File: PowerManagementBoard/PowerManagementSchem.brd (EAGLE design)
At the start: 160 x 100 mm, 29 parts, among them J1 D15S24A4GV00LF, U1 VX7805-500, U2 PYB20-Q24-S5, U3 PYB30-Q48-S5, U4 PYB30-Q48-S12, U5 3V3REG

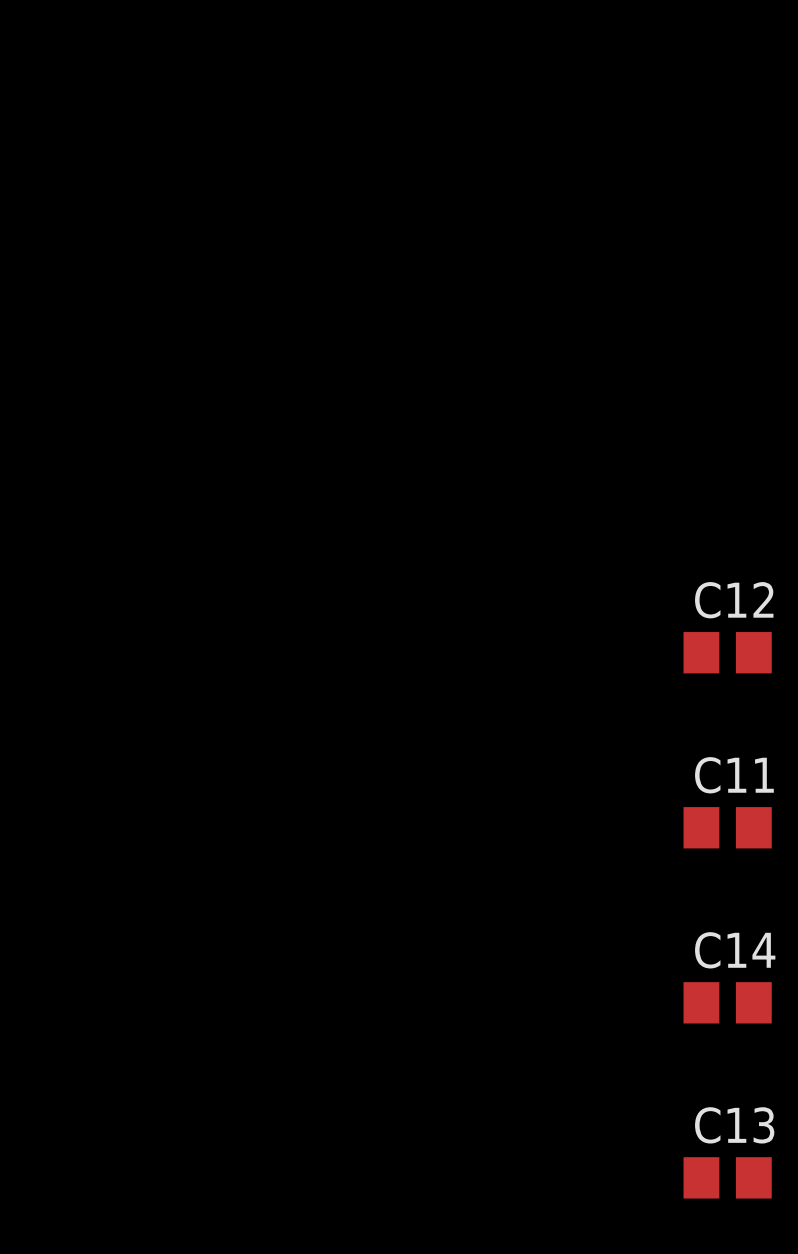
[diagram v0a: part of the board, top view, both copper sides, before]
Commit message: Added MOSFET to lib. Added Teensy to schem
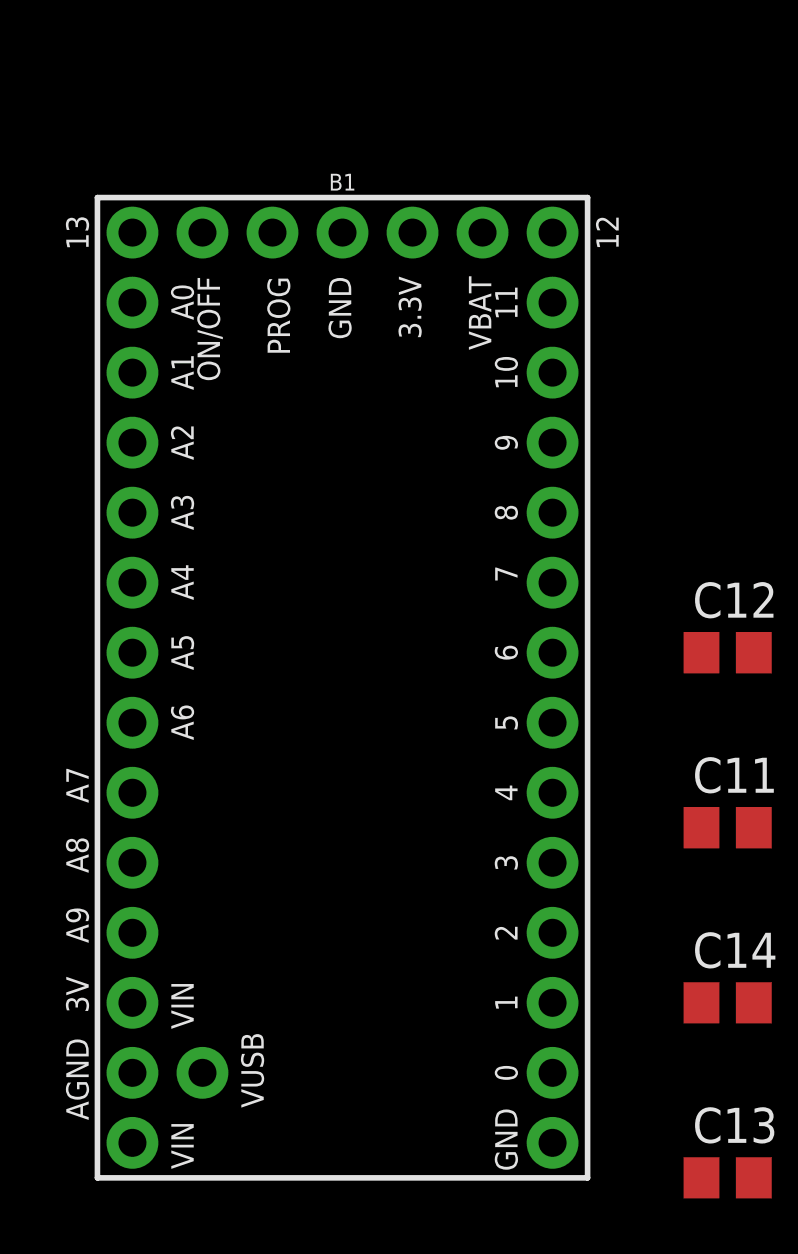
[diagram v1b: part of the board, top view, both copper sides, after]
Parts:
- added B1: TEENSY-4.0SILK, PowerManagementParts:TEENSY-4.0
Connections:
- new net 3.3V: B1.3.3V
- new net 3V: B1.3V
- new net AGND: B1.AGND
- new net GND1: B1.GND1
- new net VBAT: B1.VBAT
- new net VIN: B1.VIN
- new net VUSB: B1.VUSB
- net GND: now also B1.GND
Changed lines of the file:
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@@
 <attribute name="VALUE" x="-102.87" y="-43.18" size="1.27" layer="27"/>
+</element>
+<element name="B1" library="PowerManagementParts" package="TEENSY-4.0" package3d_urn="urn:adsk.eagle:package:37333/1" value="TEENSY-4.0SILK" x="-115.57" y="-29.21" smashed="yes">
+<attribute name="NAME" x="-115.57" y="-11.176" size="0.6096" layer="25" font="vector" ratio="20" align="bottom-center"/>
+<attribute name="SF_ID" value="DEV-12646" x="-115.57" y="-29.21" size="1.778" layer="27" display="off"/>
+<attribute name="VALUE" x="-115.57" y="-48.514" size="0.6096" layer="27" font="vector" ratio="20" align="top-center"/>
 </element>
 </elements>
@@
 <contactref element="C13" pad="2"/>
 <contactref element="C14" pad="2"/>
+<contactref element="B1" pad="GND"/>
 <wire x1="-100.65" y1="-40.64" x2="-100.65" y2="-46.99" width="0" layer="19" extent="1-1"/>
 <wire x1="-100.65" y1="-34.29" x2="-100.65" y2="-40.64" width="0" layer="19" extent="1-1"/>
 <wire x1="-100.65" y1="-27.94" x2="-100.65" y2="-34.29" width="0" layer="19" extent="1-1"/>
-<wire x1="-87.63" y1="1.27" x2="-100.65" y2="-27.94" width="0" layer="19" extent="1-1"/>
+<wire x1="-115.57" y1="-12.7" x2="-100.65" y2="-27.94" width="0" layer="19" extent="1-1"/>
+<wire x1="-87.63" y1="1.27" x2="-115.57" y2="-12.7" width="0" layer="19" extent="1-1"/>
 <wire x1="-62.23" y1="73.66" x2="-87.63" y2="1.27" width="0" layer="19" extent="1-1"/>
 <wire x1="-49.53" y1="113.03" x2="-62.23" y2="73.66" width="0" layer="19" extent="1-1"/>
@@
 <wire x1="-72.39" y1="133.909" x2="-72.39" y2="127.711" width="0" layer="19" extent="1-1"/>
 </signal>
+<signal name="GND1">
+<contactref element="B1" pad="GND1"/>
+</signal>
+<signal name="VBAT">
+<contactref element="B1" pad="VBAT"/>
+</signal>
+<signal name="3.3V">
+<contactref element="B1" pad="3.3V"/>
+</signal>
+<signal name="3V">
+<contactref element="B1" pad="3V"/>
+</signal>
+<signal name="VIN">
+<contactref element="B1" pad="VIN"/>
+</signal>
+<signal name="AGND">
+<contactref element="B1" pad="AGND"/>
+</signal>
+<signal name="VUSB">
+<contactref element="B1" pad="VUSB"/>
+</signal>
 </signals>

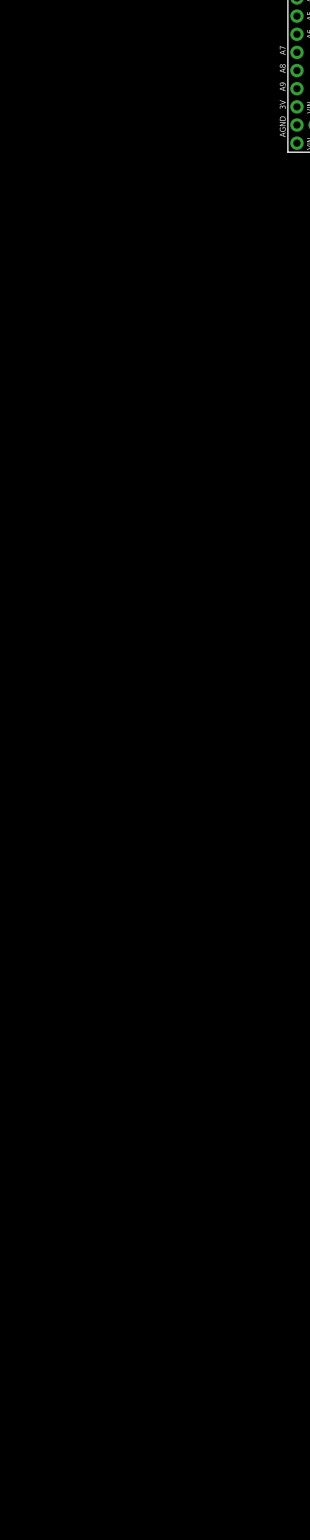
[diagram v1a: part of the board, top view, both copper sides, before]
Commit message: Created control for Laser and TX. Minor teaks to current amp part.
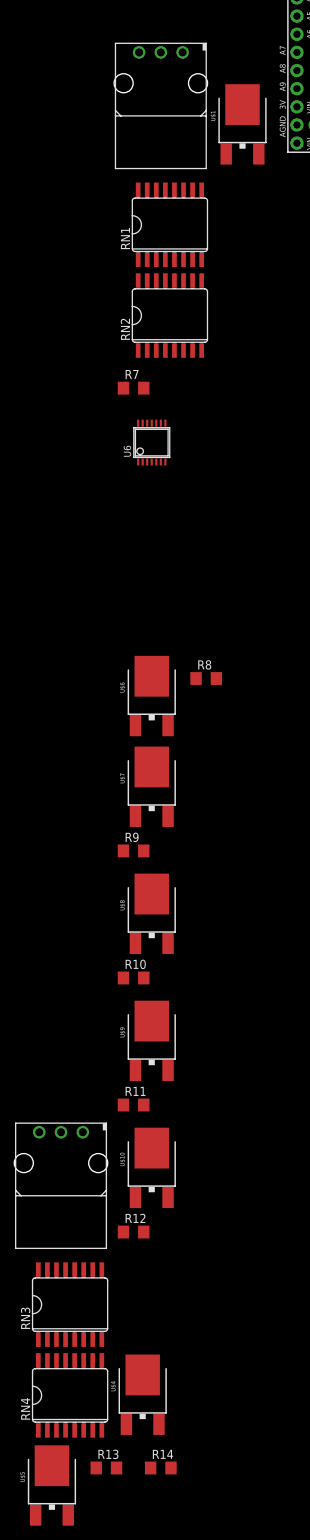
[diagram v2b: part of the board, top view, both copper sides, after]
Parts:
- added R10, R11, R12, R13, R14, R7, R8, R9: 0.01Ω, rcl:R1206
- added RN1, RN3: 100k, PowerManagementParts:SO16L
- added RN2, RN4: 100Ω, PowerManagementParts:SO16L
- added U$1, U$10, U$4, U$5, U$6, U$7, U$8, U$9: PMOSFET, usbMotorDriverParts:DPAK
- added U$2, U$3: MOLEX_3PIN, PowerManagementParts:MOLEX_3PIN
- added U6: INA4180-SPLIT, PowerManagementParts:TSSOP14
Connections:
- new net 5-ACT-LASER-EN: RN2.4
- new net 5V-ACT-LASER: R10.1, U$3.PIN2, U6.13
- new net 5V-ACT-LASER-SNS: U6.14
- new net 5V-ACT-TX: R8.1, U$2.PIN2, U6.6
- new net 5V-ACT-TX-EN: RN2.2
- new net 5V-ACT-TX-SNS: U6.7
- new net 5V-DIG-LASER: R9.1, U$3.PIN3, U6.9
- new net 5V-DIG-LASER-EN: RN2.3
- new net 5V-DIG-LASER-SNS: U6.8
- new net 5V-DIG-TX: R7.1, U$2.PIN3, U6.2
- new net 5V-DIG-TX-EN: RN2.1
- new net 5V-DIG-TX-SNS: U6.1
- new net N$10: RN1.2, RN2.15, U$6.1
- new net N$11: R7.2, U$1.4, U6.3
- new net N$12: R8.2, U$6.4, U6.5
- new net N$13: RN1.3, RN2.14, U$7.1
- new net N$14: R9.2, U$7.4, U6.10
- new net N$15: RN1.4, RN2.13, U$8.1
- new net N$16: R10.2, U$8.4, U6.12
- new net N$17: RN1.5, RN2.12, U$9.1
- new net N$18: R11.2, U$9.4
- new net N$19: RN1.6, RN2.11, U$10.1
- new net N$20: R12.2, U$10.4
- new net N$21: RN3.5, RN4.12, U$4.1
- new net N$22: R13.2, U$4.4
- new net N$23: RN3.6, RN4.11, U$5.1
- new net N$24: R14.2, U$5.4
- new net N$9: RN1.1, RN2.16, U$1.1
- net 5V-DIG: now also RN1.16, U$1.3
- net GND: now also U$2.PIN1, U$3.PIN1, U6.11
- net MNGR-3.3V: now also U6.4

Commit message: Created very rough layout of large parts on board. Added mounting holes.
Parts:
- added H1, H2, H3, H4, H5, H6: MOUNT-HOLE5.0, holes:5,0
- moved U$3 282.3 mm to (52.1, 6.35)
- moved B1 269.0 mm to (143.5, 43.2), turned to 180 degrees
- moved U$6 233.9 mm to (43.2, 19.1)
- moved U$2 178.4 mm to (31.8, 6.35)
- moved U$1 173.2 mm to (31.8, 17.8)
- moved U2 163.2 mm to (113.0, 52.1), turned to 90 degrees
- moved U5 152.5 mm to (74.9, 91.4)
- moved U3 148.4 mm to (73.7, 52.1), turned to 90 degrees
- moved U1 128.1 mm to (59.7, 90.2)
- moved J1 75.2 mm to (26.7, 90.2)
- moved U4 67.5 mm to (25.4, 52.1), turned to 90 degrees

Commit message: Updated some schem sybmols, wired up the MOSFET for cam and static
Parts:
- removed RN3: 100k, PowerManagementParts:SO16L
- removed RN4: 100Ω, PowerManagementParts:SO16L
- added R15, R16, R17, R18: 0.01Ω, rcl:R1206
- added R19: 1.2k, rcl:R0805
- added U$11, U$12: MOLEX_4PIN, PowerManagementParts:MOLEX_4PIN
- added U$13, U$14, U$15, U$16: PMOSFET, usbMotorDriverParts:DPAK
- added U$17: FLAT_LED, PowerManagementParts:FLAT_LED
- added U$18, U$19: CD4051B_ALT, PowerManagementParts:SOIC16N
- added U7: INA4180-SPLIT, PowerManagementParts:TSSOP14
- R11, R12: value 0.01Ω -> 330; device rcl:R1206 -> rcl:R0805
- U$10, U$9: value PMOSFET -> FLAT_LED; device usbMotorDriverParts:DPAK -> PowerManagementParts:FLAT_LED
- moved U$9 296.3 mm to (-158.8, -466.1)
- moved R11 296.2 mm to (-160.0, -476.2)
- moved R12 283.6 mm to (-160.0, -481.3)
- moved U$10 281.1 mm to (-158.8, -468.6)
- renumbered B1 to U8
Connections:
- removed net N$20: R12.2, U$10.4
- new net 12V-CAM: U$11.PIN1
- new net 12V-STA: U$12.PIN1
- new net 5V-ACT-CAM: R17.1, U$11.PIN3, U7.6
- new net 5V-ACT-CAM-EN: RN2.6
- new net 5V-ACT-CAM-SNS: U7.7
- new net 5V-ACT-LASER-EN: U8.5
- new net 5V-ACT-STA: R15.1, U$12.PIN3, U7.13
- new net 5V-ACT-STA-EN: RN2.8
- new net 5V-ACT-STA-SNS: U7.14
- new net 5V-DIG-CAM: R18.1, U$11.PIN4, U7.2
- new net 5V-DIG-CAM-EN: RN2.5
- new net 5V-DIG-CAM-SNS: U7.1
- new net 5V-DIG-STA: R16.1, U$12.PIN4, U7.9
- new net 5V-DIG-STA-EN: RN2.7
- new net 5V-DIG-STA-SNS: U7.8
- new net CURRENT-SNS-A: U$18.3, U8.22
- new net CURRENT-SNS-B: U$19.3, U8.23
- new net N$25: RN1.8, RN2.9, U$13.1
- new net N$26: R15.2, U$13.4, U7.12
- new net N$27: RN1.7, RN2.10, U$14.1
- new net N$28: R16.2, U$14.4, U7.10
- new net N$29: RN1.6, RN2.11, U$15.1
- new net N$30: R17.2, U$15.4, U7.5
- new net N$31: RN1.5, RN2.12, U$16.1
- new net N$32: R18.2, U$16.4, U7.3
- new net N$36: U8.6
- new net N$37: U8.7
- new net N$38: U8.8
- new net N$39: U8.9
- new net N$40: U8.10
- net 12V: now also U$17.ANODE
- net 5V-ACT: now also RN1.11, RN1.13, RN1.15, RN1.9, U$10.ANODE, U$13.3, U$15.3, U$6.3, U$8.3
- net 5V-ACT-TX-EN: now also U8.3
- net 5V-DIG: now also RN1.10, RN1.12, RN1.14, U$14.3, U$16.3, U$7.3, U$9.ANODE
- net 5V-DIG-LASER-EN: now also U8.4
- net 5V-DIG-TX-EN: now also U8.2
- net GND: now also R11.1, R12.1, R19.1, U$11.PIN2, U$12.PIN2, U7.11
- net MNGR-3.3V: now also U7.4
- net N$17: now also R11.2, U$9.CATHODE; no longer RN1.5, RN2.12, U$9.1
- net N$18: now also R12.2, U$10.CATHODE; no longer R11.2, U$9.4
- net N$19: now also R19.2, U$17.CATHODE; no longer RN1.6, RN2.11, U$10.1
- net N$21: no longer RN3.5, RN4.12
- net N$23: no longer RN3.6, RN4.11

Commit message: Added notes and minor changes
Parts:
- added D1, D10, D11, D12, D2, D3, D4, D5, D6, D7, D8, D9: S1M, diode:SMA
- added R20, R21: 0.01Ω, rcl:R1206
- added R22: 330, rcl:R0805
- added RN3: 100Ω, PowerManagementParts:SO16L
- added RN4: 100kΩ, PowerManagementParts:SO16L
- added U$20: FLAT_LED, PowerManagementParts:FLAT_LED
- added U$22, U$23: PMOSFET, usbMotorDriverParts:DPAK
- added U$24: MOLEX_3PIN, PowerManagementParts:MOLEX_3PIN
- added U9: INA4180-SPLIT, PowerManagementParts:TSSOP14
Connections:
- net N$38 renamed 12V-CAM-EN
- removed net N$39: U8.9
- new net 12V-CAM-SNS: U$18.5
- new net 12V-STA-EN: U8.16
- new net 12V-STA-SNS: U$19.5
- new net 5V-ACT-MAG: R13.1, U$24.PIN2, U9.6
- new net 5V-ACT-MAG-EN: RN3.2, U8.10
- new net 5V-ACT-MAG-SNS: U$19.12, U9.7
- new net 5V-DIG-MAG: R14.1, U$24.PIN3, U9.2
- new net 5V-DIG-MAG-EN: RN3.1, U8.9
- new net 5V-DIG-MAG-SNS: U$18.12, U9.1
- new net MUX-SEL-A: U$18.11, U$19.11, U8.17
- new net MUX-SEL-B: U$18.10, U$19.10, U8.20
- new net MUX-SEL-C: U$18.9, U$19.9, U8.21
- new net N$20: R22.2, U$20.CATHODE
- new net N$34: R20.2, U$22.4, U9.10
- new net N$35: R20.1, U9.9
- new net N$41: RN4.14, U$22.3
- new net N$42: RN4.13, U$23.3
- new net N$43: RN3.13, RN4.4, U$23.1
- net 5V-ACT: now also D10.C, D2.C, D4.C, D6.C, D8.C, RN4.15, U$4.3
- net 5V-ACT-CAM-EN: now also U8.7
- net 5V-ACT-CAM-SNS: now also U$19.15
- net 5V-ACT-LASER-SNS: now also U$19.14
- net 5V-ACT-STA-EN: now also U8.15
- net 5V-ACT-STA-SNS: now also U$19.1
- net 5V-ACT-TX-SNS: now also U$19.13
- net 5V-DIG: now also D3.C, D5.C, D7.C, D9.C, RN4.16, U$5.3
- net 5V-DIG-CAM-EN: now also U8.6
- net 5V-DIG-CAM-SNS: now also U$18.15
- net 5V-DIG-LASER-SNS: now also U$18.14
- net 5V-DIG-STA-EN: now also U8.14
- net 5V-DIG-STA-SNS: now also U$18.1
- net 5V-DIG-TX-SNS: now also U$18.13
- net GND: now also R22.1, U$18.7, U$18.8, U$19.7, U$19.8, U$24.PIN1, U9.11
- net MNGR-3.3V: now also U$18.16, U$19.16, U9.4
- net MNGR-5V: now also U$20.ANODE
- net N$12: now also D2.A
- net N$14: now also D3.A
- net N$16: now also D4.A
- net N$21: now also RN3.15, RN4.2
- net N$22: now also D10.A, U9.5
- net N$23: now also RN3.16, RN4.1
- net N$24: now also D9.A, U9.3
- net N$26: now also D8.A
- net N$28: now also D7.A
- net N$30: now also D6.A
- net N$32: now also D5.A
- net N$36: now also R21.2, U$23.4, U9.12; no longer U8.6
- net N$37: now also R21.1, U9.13; no longer U8.7
- net N$40: now also RN3.14, RN4.3, U$22.1; no longer U8.10

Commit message: Test: tried changing hole diameter on this branch while other branch is modified
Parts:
- added U$21: FLAT_LED, PowerManagementParts:FLAT_LED
- H1, H2, H3, H4, H5, H6: value MOUNT-HOLE5.0 -> MOUNT-HOLE3.0; device holes:5,0 -> holes:3,0
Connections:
- removed net 3.3V: U8.3.3V
- removed net N$41: RN4.14, U$22.3
- new net N$33: RN3.3
- net 12V: now also RN4.14, U$22.3
- net 12V-CAM-SNS: now also U9.8
- net MNGR-3.3V: now also U8.3.3V
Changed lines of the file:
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@@
 <attribute name="VALUE" x="-143.51" y="-233.68" size="1.27" layer="27"/>
 </element>
-<element name="H1" library="holes" library_urn="urn:adsk.eagle:library:237" package="5,0" package3d_urn="urn:adsk.eagle:package:14276/1" value="MOUNT-HOLE5.0" x="-154.94" y="-246.38" smashed="yes"/>
-<element name="H2" library="holes" library_urn="urn:adsk.eagle:library:237" package="5,0" package3d_urn="urn:adsk.eagle:package:14276/1" value="MOUNT-HOLE5.0" x="-154.94" y="-260.35" smashed="yes"/>
-<element name="H3" library="holes" library_urn="urn:adsk.eagle:library:237" package="5,0" package3d_urn="urn:adsk.eagle:package:14276/1" value="MOUNT-HOLE5.0" x="-154.94" y="-274.32" smashed="yes"/>
-<element name="H4" library="holes" library_urn="urn:adsk.eagle:library:237" package="5,0" package3d_urn="urn:adsk.eagle:package:14276/1" value="MOUNT-HOLE5.0" x="-154.94" y="-288.29" smashed="yes"/>
-<element name="H5" library="holes" library_urn="urn:adsk.eagle:library:237" package="5,0" package3d_urn="urn:adsk.eagle:package:14276/1" value="MOUNT-HOLE5.0" x="-154.94" y="-302.26" smashed="yes"/>
-<element name="H6" library="holes" library_urn="urn:adsk.eagle:library:237" package="5,0" package3d_urn="urn:adsk.eagle:package:14276/1" value="MOUNT-HOLE5.0" x="-154.94" y="-316.23" smashed="yes"/>
+<element name="H1" library="holes" library_urn="urn:adsk.eagle:library:237" package="3,0" package3d_urn="urn:adsk.eagle:package:14277/1" value="MOUNT-HOLE3.0" x="-154.94" y="-246.38" smashed="yes"/>
+<element name="H2" library="holes" library_urn="urn:adsk.eagle:library:237" package="3,0" package3d_urn="urn:adsk.eagle:package:14277/1" value="MOUNT-HOLE3.0" x="-154.94" y="-260.35" smashed="yes"/>
+<element name="H3" library="holes" library_urn="urn:adsk.eagle:library:237" package="3,0" package3d_urn="urn:adsk.eagle:package:14277/1" value="MOUNT-HOLE3.0" x="-154.94" y="-274.32" smashed="yes"/>
+<element name="H4" library="holes" library_urn="urn:adsk.eagle:library:237" package="3,0" package3d_urn="urn:adsk.eagle:package:14277/1" value="MOUNT-HOLE3.0" x="-154.94" y="-288.29" smashed="yes"/>
+<element name="H5" library="holes" library_urn="urn:adsk.eagle:library:237" package="3,0" package3d_urn="urn:adsk.eagle:package:14277/1" value="MOUNT-HOLE3.0" x="-154.94" y="-302.26" smashed="yes"/>
+<element name="H6" library="holes" library_urn="urn:adsk.eagle:library:237" package="3,0" package3d_urn="urn:adsk.eagle:package:14277/1" value="MOUNT-HOLE3.0" x="-154.94" y="-316.23" smashed="yes"/>
 <element name="U$13" library="usbMotorDriverParts" package="DPAK" package3d_urn="urn:adsk.eagle:package:38459/1" value="PMOSFET" x="-157.48" y="-364.49"/>
 <element name="R15" library="rcl" library_urn="urn:adsk.eagle:library:334" package="R1206" package3d_urn="urn:adsk.eagle:package:23540/2" value="0.01Ω" x="-149.86" y="-374.65">
@@
 <attribute name="SPICEPREFIX" value="R" x="-261.62" y="-589.28" size="1.778" layer="27" display="off"/>
 </element>
+<element name="U$21" library="PowerManagementParts" package="FLAT_LED" value="FLAT_LED" x="-261.62" y="-593.09"/>
 </elements>
 <signals>
@@
 <contactref element="C6" pad="1"/>
 <contactref element="U$17" pad="ANODE"/>
+<contactref element="RN4" pad="14"/>
+<contactref element="U$22" pad="3"/>
+<wire x1="-242.83" y1="-551.41" x2="-226.695" y2="-529.7678" width="0" layer="19" extent="1-1"/>
+<wire x1="-158.75" y1="-471.17" x2="-226.695" y2="-529.7678" width="0" layer="19" extent="1-1"/>
 <wire x1="30.48" y1="74.93" x2="-158.75" y2="-471.17" width="0" layer="19" extent="1-1"/>
 <wire x1="-34.61" y1="149.86" x2="30.48" y2="74.93" width="0" layer="19" extent="1-1"/>
@@
 <contactref element="U$18" pad="16"/>
 <contactref element="U9" pad="4"/>
+<contactref element="U8" pad="3.3V"/>
 <wire x1="-159.385" y1="-501.59" x2="-228.6" y2="-514.5278" width="0" layer="19" extent="1-1"/>
 <wire x1="-159.385" y1="-492.7" x2="-159.385" y2="-501.59" width="0" layer="19" extent="1-1"/>
@@
 <wire x1="74.93" y1="88.341" x2="-102.55" y2="-40.64" width="0" layer="19" extent="1-1"/>
 <wire x1="74.93" y1="94.539" x2="74.93" y2="88.341" width="0" layer="19" extent="1-1"/>
+<wire x1="140.97" y1="26.67" x2="74.93" y2="88.341" width="0" layer="19" extent="1-1"/>
 </signal>
 <signal name="GND1">
@@
 <signal name="VBAT">
 <contactref element="U8" pad="VBAT"/>
-</signal>
-<signal name="3.3V">
-<contactref element="U8" pad="3.3V"/>
 </signal>
 <signal name="3V">
@@
 <signal name="12V-CAM-SNS">
 <contactref element="U$18" pad="5"/>
+<contactref element="U9" pad="8"/>
+<wire x1="-154.305" y1="-497.9" x2="-226.695" y2="-509.0922" width="0" layer="19" extent="1-1"/>
 </signal>
 <signal name="12V-STA-SNS">
@@
 <wire x1="-247.39" y1="-551.41" x2="-226.695" y2="-539.5722" width="0" layer="19" extent="1-1"/>
 </signal>
-<signal name="N$41">
-<contactref element="RN4" pad="14"/>
-<contactref element="U$22" pad="3"/>
-<wire x1="-242.83" y1="-551.41" x2="-226.695" y2="-529.7678" width="0" layer="19" extent="1-1"/>
-</signal>
 <signal name="N$42">
 <contactref element="RN4" pad="13"/>
@@
 <wire x1="-260.67" y1="-585.47" x2="-259.08" y2="-590.55" width="0" layer="19" extent="1-1"/>
 </signal>
+<signal name="N$33">
+<contactref element="RN3" pad="3"/>
+</signal>
 </signals>
